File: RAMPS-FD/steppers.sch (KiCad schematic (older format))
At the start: 16 parts, among them P201 3 2 1, P202 3 2 1, P203 3 2 1, P204 X, P205 Y, P206 Z1, P3 Z2, U201 X, U202 Y, U203 Z

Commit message: Changed fuse holders to Keystone 3568; specificy HCT instead of ACT logic
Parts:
- P201, P202, P203: footprint pin_array:pin_array_3x2 -> Pin_Headers:Pin_Header_Straight_2x03
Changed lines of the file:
@@
 F 0 "P202" H 2250 6975 50  0000 C CNN
 F 1 "3 2 1" V 2250 6775 40  0000 C CNN
-F 2 "pin_array:pin_array_3x2" H 2250 6725 60  0001 C CNN
+F 2 "Pin_Headers:Pin_Header_Straight_2x03" H 2250 6725 60  0001 C CNN
 F 3 "" H 2250 6725 60  0001 C CNN
 	1    2250 6725
@@
 F 0 "P201" H 2250 4625 50  0000 C CNN
 F 1 "3 2 1" V 2250 4425 40  0000 C CNN
-F 2 "pin_array:pin_array_3x2" H 2250 4375 60  0001 C CNN
+F 2 "Pin_Headers:Pin_Header_Straight_2x03" H 2250 4375 60  0001 C CNN
 F 3 "" H 2250 4375 60  0001 C CNN
 	1    2250 4375
@@
 F 0 "P203" H 2250 2275 50  0000 C CNN
 F 1 "3 2 1" V 2250 2075 40  0000 C CNN
-F 2 "pin_array:pin_array_3x2" H 2250 2025 60  0001 C CNN
+F 2 "Pin_Headers:Pin_Header_Straight_2x03" H 2250 2025 60  0001 C CNN
 F 3 "" H 2250 2025 60  0001 C CNN
 	1    2250 2025

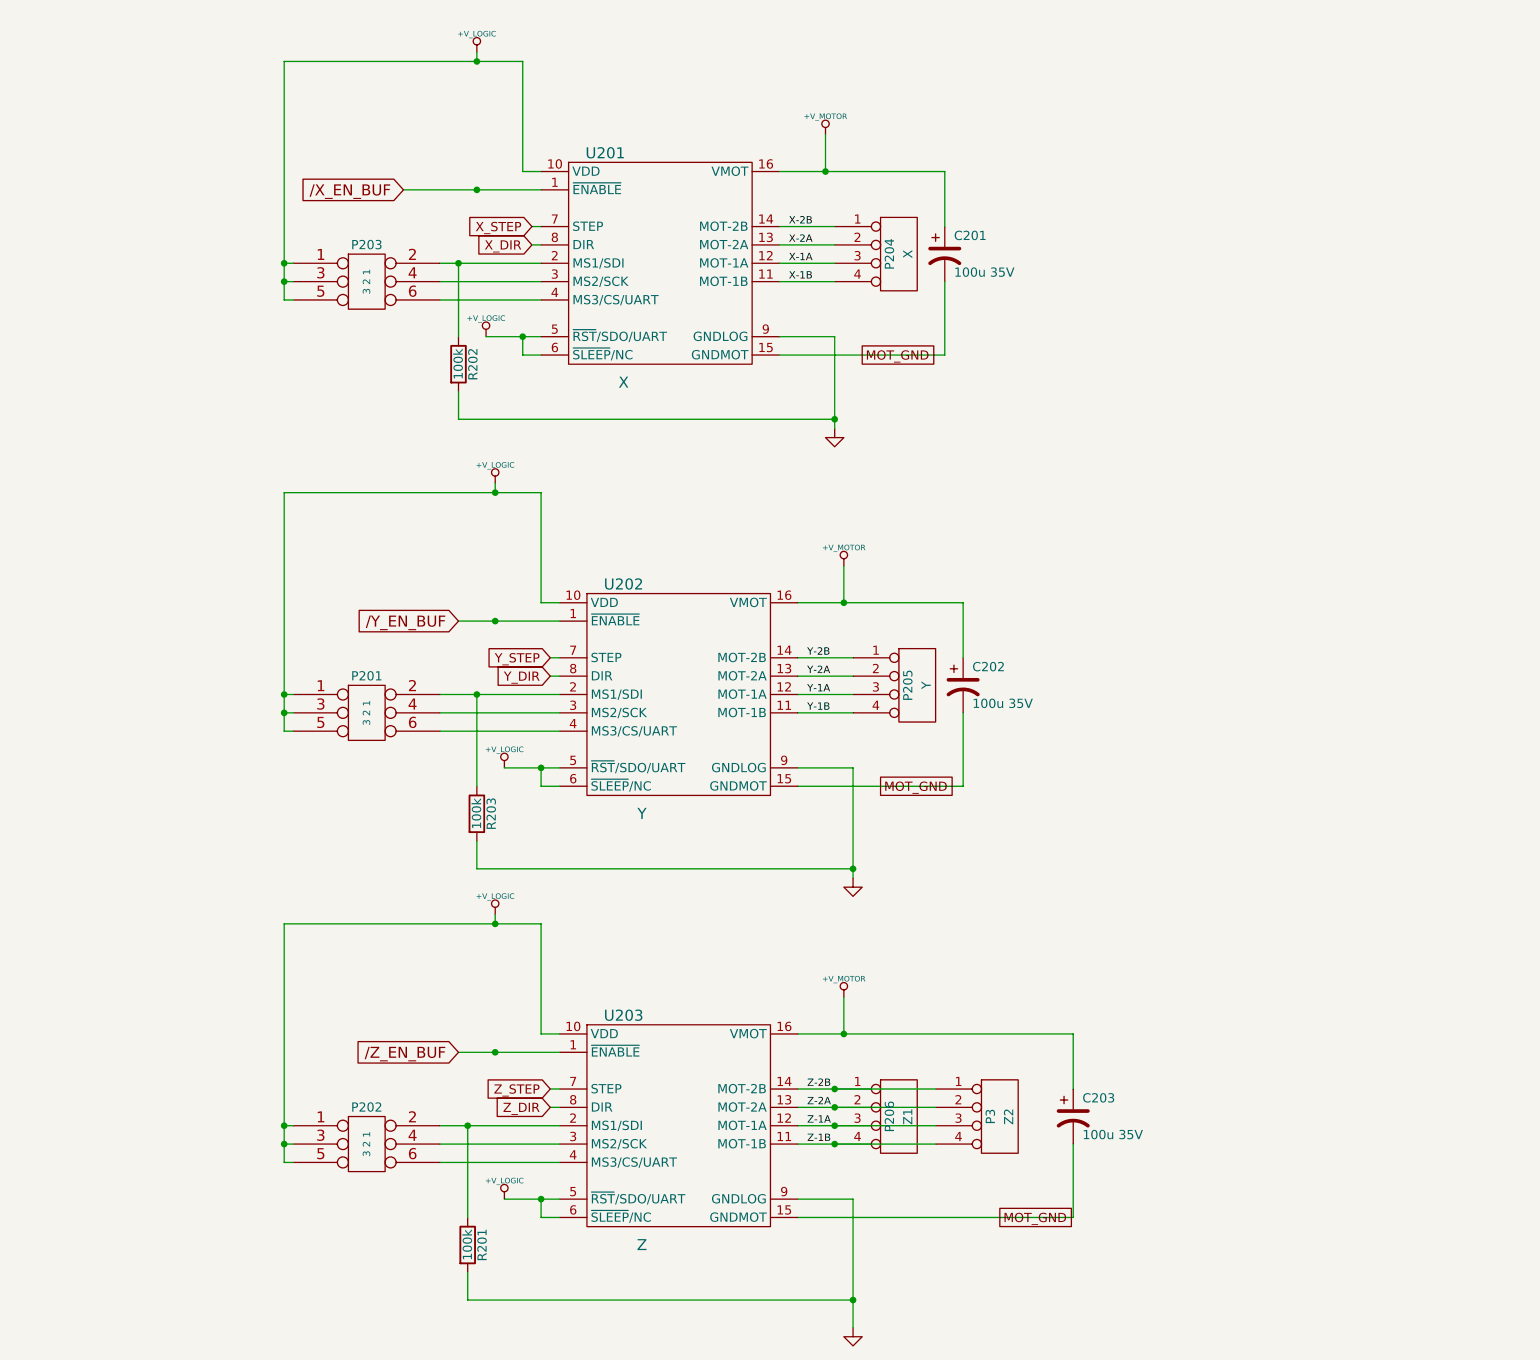
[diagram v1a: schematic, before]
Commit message: Fix 3d view; remove faulty ADC protection
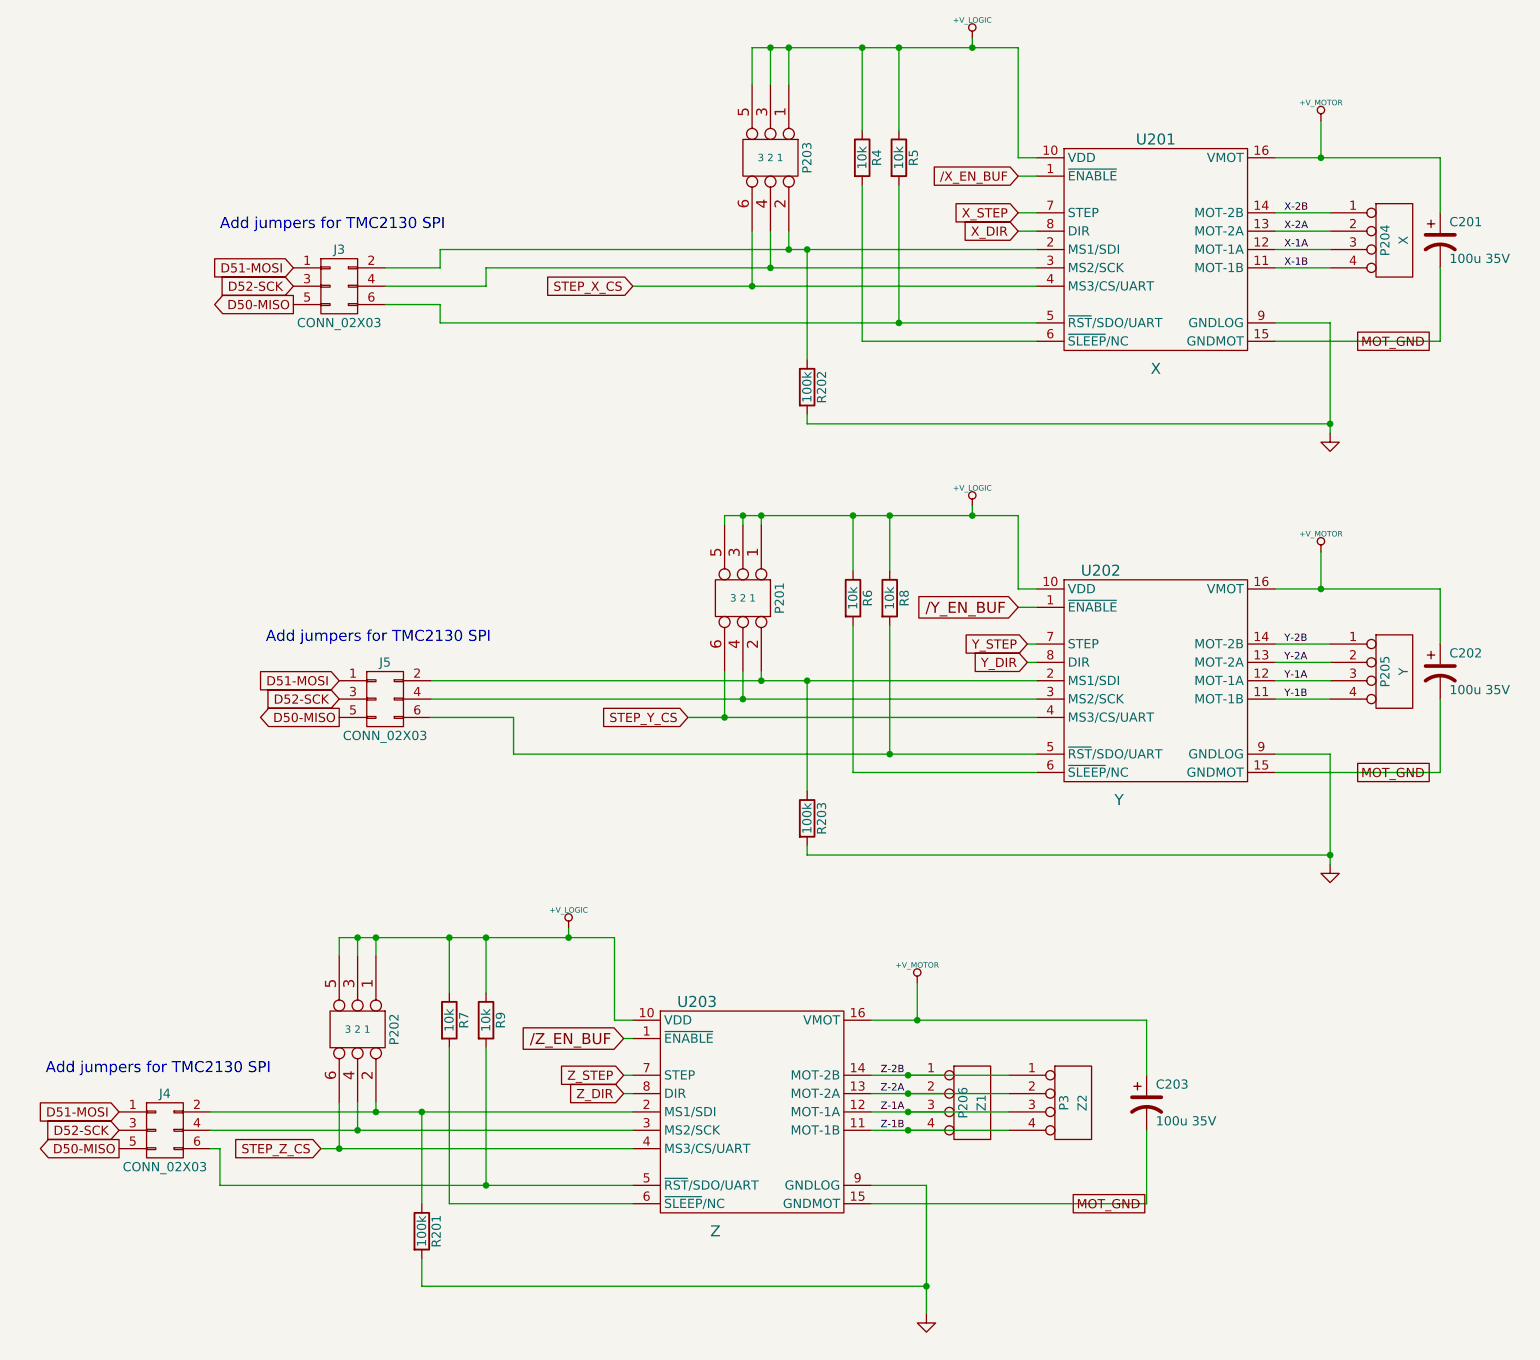
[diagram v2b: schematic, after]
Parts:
- added J3, J4, J5: CONN_02X03, Pin_Headers:Pin_Header_Straight_2x03_Pitch2.54mm, symbol CONN_02X03
- added R4, R5, R6, R7, R8, R9: 10k, Resistors_SMD:R_0603, symbol R
- C201, C202, C203: footprint Capacitors_SMD:c_elec_6.3x7.7 -> Capacitors_SMD:CP_Elec_6.3x7.7
- P201, P202, P203: footprint Pin_Headers:Pin_Header_Straight_2x03 -> Pin_Headers:Pin_Header_Straight_2x03_Pitch2.54mm
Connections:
- net +V_LOGIC: now also R4.1, R5.1, R6.1, R7.1, R8.1, R9.1; no longer U201.5 (~RST~/SDO/UART), U201.6 (~SLEEP~/NC), U202.5 (~RST~/SDO/UART), U202.6 (~SLEEP~/NC), U203.5 (~RST~/SDO/UART), U203.6 (~SLEEP~/NC)
- net at P203.2, R202.1, U201.2 (MS1/SDI): now also J3.2 (P2)
- net at P203.4, U201.3 (MS2/SCK): now also J3.4 (P4)
- net STEP_X_CS: now reaches P203.6, U201.4 (MS3/CS/UART)
- net at P201.2, R203.1, U202.2 (MS1/SDI): now also J5.2 (P2)
- net at P201.4, U202.3 (MS2/SCK): now also J5.4 (P4)
- net STEP_Y_CS: now reaches P201.6, U202.4 (MS3/CS/UART)
- net at P202.2, R201.1, U203.2 (MS1/SDI): now also J4.2 (P2)
- net at P202.4, U203.3 (MS2/SCK): now also J4.4 (P4)
- net STEP_Z_CS: now reaches P202.6, U203.4 (MS3/CS/UART)
- new net: J3.6 (P6), R5.2, U201.5 (~RST~/SDO/UART)
- new net: R4.2, U201.6 (~SLEEP~/NC)
- new net: J5.6 (P6), R8.2, U202.5 (~RST~/SDO/UART)
- new net: R6.2, U202.6 (~SLEEP~/NC)
- new net: J4.6 (P6), R9.2, U203.5 (~RST~/SDO/UART)
- new net: R7.2, U203.6 (~SLEEP~/NC)
- new net D50-MISO: J3.5 (P5), J4.5 (P5), J5.5 (P5)
- new net D51-MOSI: J3.1 (P1), J4.1 (P1), J5.1 (P1)
- new net D52-SCK: J3.3 (P3), J4.3 (P3), J5.3 (P3)
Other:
- note added: "Add jumpers for TMC2130 SPI"
- moved on the sheet: C201, C202, C203, P201, P202, P203, P204, P205, P206, P3, R201, R202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
